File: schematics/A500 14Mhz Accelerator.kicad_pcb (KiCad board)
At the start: 2 copper layers, 120.6 x 54.6 mm, 17 parts, among them J1 Speed Selector, U1 68000 Boardside, U10 74HC74, U2 68HC000 Socket, U3 74HC86, U4 74HC74, U5 74LS27, U6 74LS112, U7 74HC04, U8 74LS157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

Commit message: Add files via upload
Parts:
- added C10: 0.1uF, Capacitor_THT:C_Axial_L3.8mm_D2.6mm_P7.50mm_Horizontal, F.Cu at (192.4, 130.2)
- added C4: 0.1uF, Capacitor_THT:C_Axial_L3.8mm_D2.6mm_P7.50mm_Horizontal, F.Cu at (182.2, 123.8)
- added C5: 0.1uF, Capacitor_THT:C_Axial_L3.8mm_D2.6mm_P7.50mm_Horizontal, F.Cu at (182.2, 127.0)
- added C6: 0.1uF, Capacitor_THT:C_Axial_L3.8mm_D2.6mm_P7.50mm_Horizontal, F.Cu at (182.2, 130.2)
- added C7: 0.1uF, Capacitor_THT:C_Axial_L3.8mm_D2.6mm_P7.50mm_Horizontal, F.Cu at (182.2, 133.3)
- added C8: 0.1uF, Capacitor_THT:C_Axial_L3.8mm_D2.6mm_P7.50mm_Horizontal, F.Cu at (192.4, 123.8)
- added C9: 0.1uF, Capacitor_THT:C_Axial_L3.8mm_D2.6mm_P7.50mm_Horizontal, F.Cu at (192.4, 127.0)
- C1: value 0.1uF -> 22pf
- C3: value 22pf -> 0.1uF
- moved C1 18.6 mm to (172.2, 132.7)
- moved C2 18.6 mm to (172.2, 135.9)
- moved U2 17.2 mm to (200.7, 102.9), turned to 270 degrees
- moved C3 13.2 mm to (179.7, 139.1), turned to 180 degrees
- moved J1 2.69 mm to (203.2, 128.9)
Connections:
- C1 pad 1: /VCC -> /GND
- C1 pad 2: /GND -> Net-(C1-Pad2)
- C2 pad 2: Net-(C2-Pad2) -> /A500 14Mhz Accelerator Sheet 2/CDAC
- C3 pad 1: /GND -> /VCC
- C3 pad 2: /A500 14Mhz Accelerator Sheet 2/CDAC -> /GND
- R1 pad 1: Net-(C2-Pad2) -> Net-(C1-Pad2)
- R2 pad 2: Net-(C2-Pad2) -> Net-(C1-Pad2)
- U3 pad 4: Net-(C2-Pad2) -> Net-(C1-Pad2)
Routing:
- net /CPU_A11: track 152.2 -> 81.9 mm, vias 2 -> 0
- net /CPU_A13: track 144.6 -> 76.8 mm
- net /CPU_E: track 153.9 -> 97.3 mm
- net /CPU_HALT: track 59.0 -> 99.3 mm, vias 0 -> 1
- net /CPU_DTACK14: track 54.1 -> 92.3 mm, vias 1 -> 0
- net Net-(C2-Pad2): track 37.8 -> 0.00 mm
- net /CPU_A17: track 107.3 -> 70.2 mm, vias 1 -> 0
- net /CPU_A19: track 104.9 -> 68.2 mm, vias 1 -> 0
- net /CPU_A15: track 111.1 -> 75.6 mm, vias 2 -> 0
- net /CPU_A16: track 102.6 -> 71.2 mm
- net Net-(C1-Pad2): track 0.00 -> 30.8 mm
- net /CPU_A4: track 124.7 -> 94.4 mm
- net /CPU_A22: track 95.2 -> 65.3 mm
- net /CPU_VPA14: track 104.4 -> 75.1 mm, vias 2 -> 0
- net /CPU_D4: track 22.4 -> 50.8 mm
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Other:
- board size 120.6 x 54.6 mm -> 121.9 x 55.9 mm
- board text added: "1"
- board text added: "14Mhz Accelerator (C) 1992 Livio Plos"
- board text added: "Hello Cave Dwellers!"

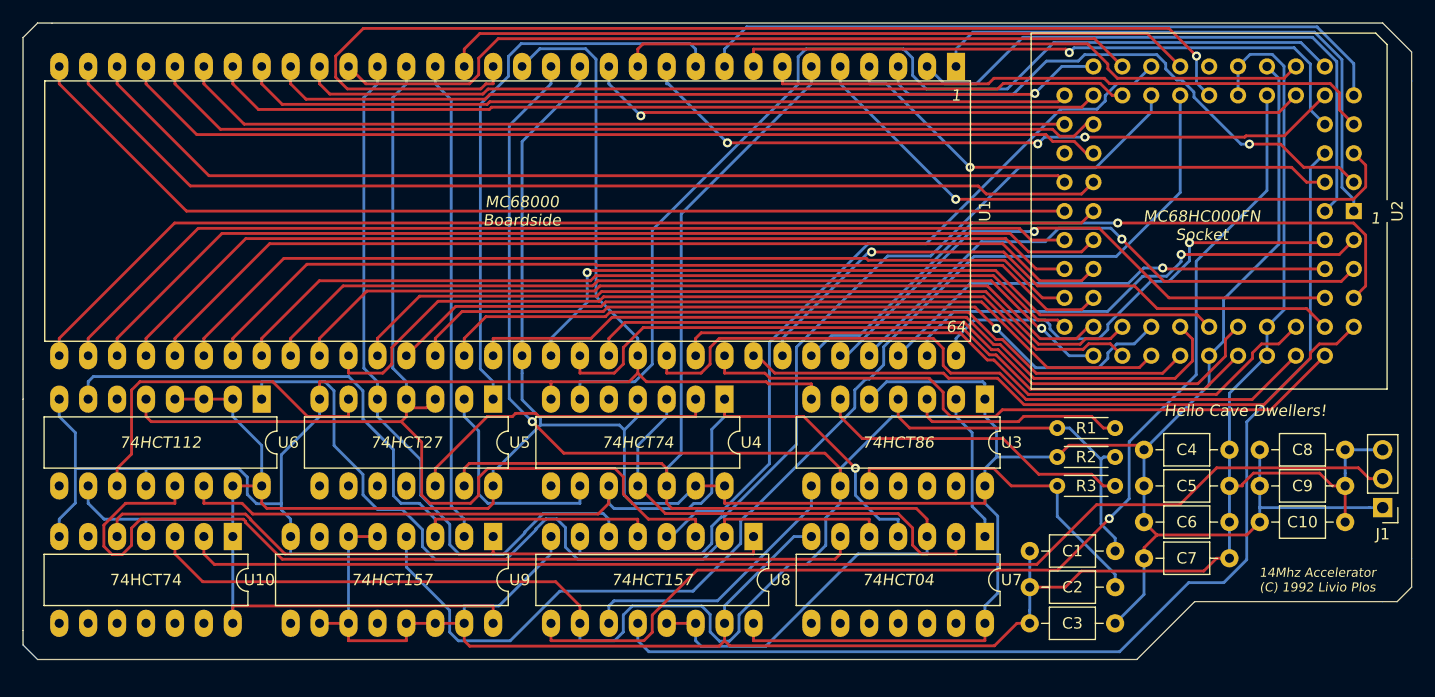
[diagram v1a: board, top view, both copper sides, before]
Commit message: Respin to add copper fill
Moved components around for better decoupling on the caps, added copper fill
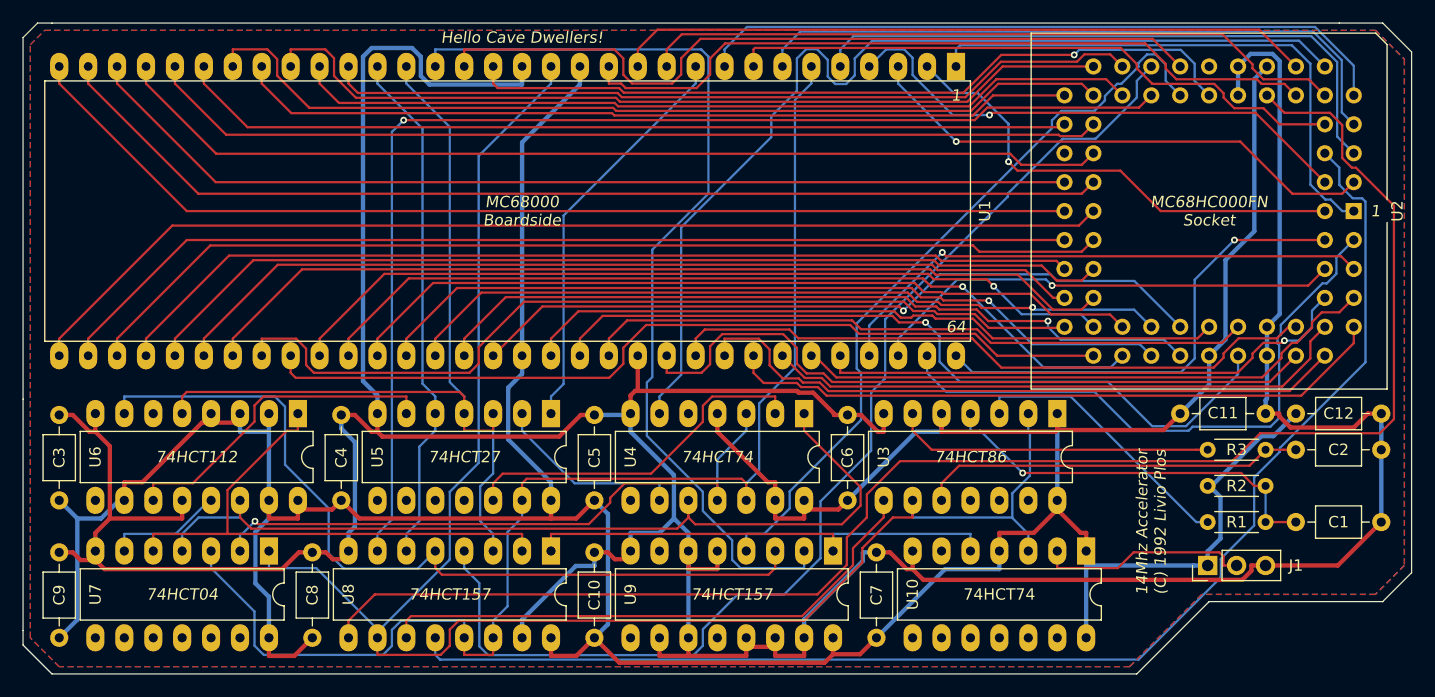
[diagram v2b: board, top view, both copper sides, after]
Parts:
- added C11: 0.1uF, Capacitor_THT:C_Axial_L3.8mm_D2.6mm_P7.50mm_Horizontal, F.Cu at (185.4, 120.7)
- added C12: 0.1uF, Capacitor_THT:C_Axial_L3.8mm_D2.6mm_P7.50mm_Horizontal, F.Cu at (195.6, 120.7)
- moved C9 106.3 mm to (87.0, 140.3), turned to 90 degrees
- moved C3 93.3 mm to (87.0, 128.3), turned to 90 degrees
- moved C8 84.8 mm to (109.2, 140.3), turned to 90 degrees
- moved U10 74.9 mm to (177.2, 132.7)
- moved C4 70.6 mm to (111.8, 128.3), turned to 90 degrees
- moved U7 62.9 mm to (105.4, 132.7)
- moved C10 59.3 mm to (134.0, 140.3), turned to 90 degrees
- moved C5 48.3 mm to (134.0, 128.3), turned to 90 degrees
- moved C2 33.1 mm to (203.1, 123.8), turned to 180 degrees
- moved C1 31.0 mm to (203.1, 130.2), turned to 180 degrees
- moved U9 29.9 mm to (154.9, 132.7)
- moved C6 26.1 mm to (156.2, 128.3), turned to 90 degrees
- moved C7 24.5 mm to (158.8, 140.3), turned to 90 degrees
- moved R1 20.1 mm to (192.9, 130.2), turned to 180 degrees
- moved R3 18.6 mm to (192.9, 123.8), turned to 180 degrees
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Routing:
- net /A500 14Mhz Accelerator Sheet 2/SPD_SEL: track 109.3 -> 18.8 mm
- net /A500 14Mhz Accelerator Sheet 2/_E_OUT: track 80.8 -> 10.3 mm
- net /CPU_VMA: track 42.3 -> 83.4 mm
- net /CPU_CLK14: track 98.8 -> 138.8 mm, vias 1 -> 0
- net /CPU_VMA14: track 102.3 -> 66.6 mm
- net /CPU_E14: track 66.2 -> 100.5 mm
- net /CPU_HALT: track 99.3 -> 68.8 mm
- net /CPU_VPA14: track 75.1 -> 105.3 mm, vias 0 -> 1
- net /A500 14Mhz Accelerator Sheet 2/SW_E14: track 74.0 -> 49.1 mm
- net /A500 14Mhz Accelerator Sheet 2/SW_CLK14: track 24.8 -> 49.5 mm
- net /CPU_AS14: track 97.3 -> 118.1 mm
- net /GND: track 342.9 -> 363.4 mm
- net /A500 14Mhz Accelerator Sheet 2/SEL_SW: track 62.1 -> 42.8 mm
- net /CPU_CLK: track 168.5 -> 150.0 mm, vias 1 -> 0
- net /CPU_E: track 97.3 -> 79.2 mm
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- added copper zone on F.Cu, net /GND
- added copper zone on B.Cu, net /VCC
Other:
- board size 121.9 x 55.9 mm -> 121.9 x 57.1 mm
- net class Default: trace_width 0.25 -> 0.2; via_dia 0.8 -> 0.6; via_drill 0.4 -> 0.3
- net class Power added: clearance 0.2, trace_width 0.381, via_dia 0.8, via_drill 0.4
- rule via_min_drill: 0.3 -> 0.2

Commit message: Reroute with correct socket
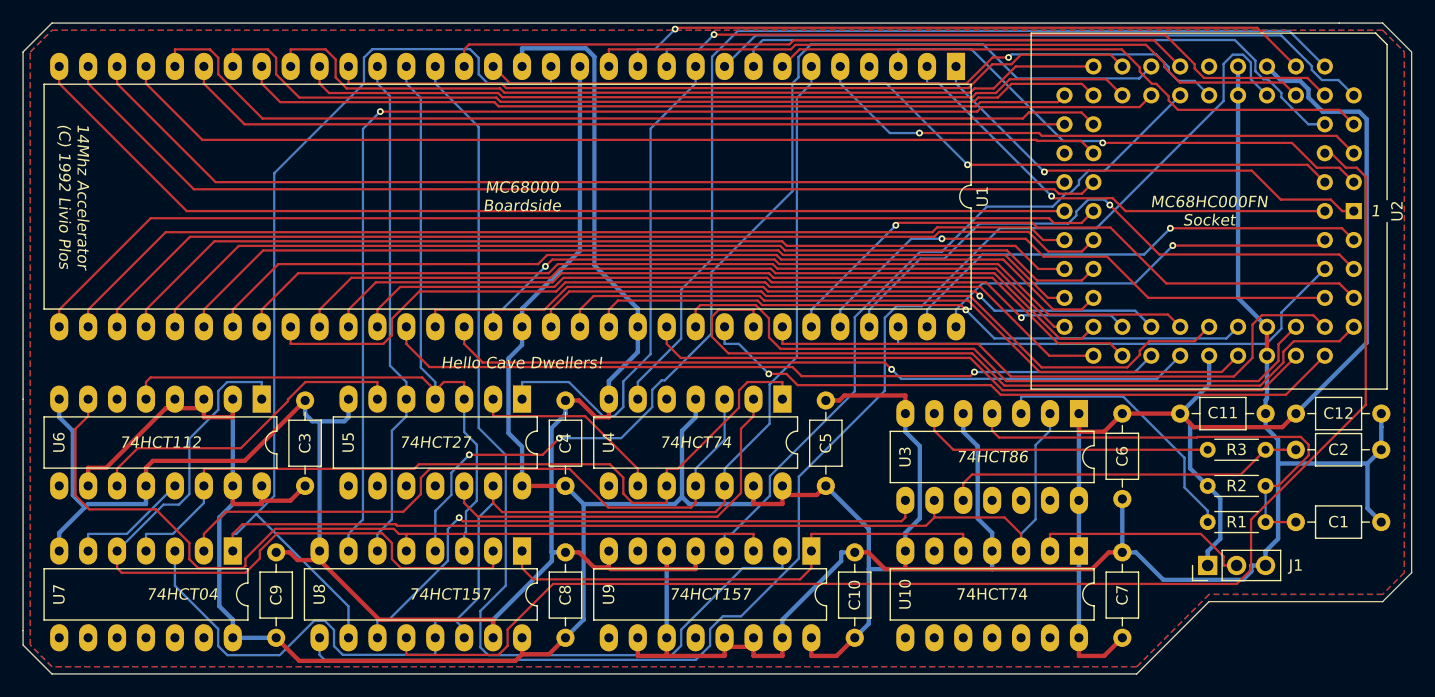
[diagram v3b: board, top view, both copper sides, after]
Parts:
- U1: footprint Package_DIP:DIP-64_W25.4mm_SIL_Headers -> Package_DIP:DIP-64_W22.86mm_LongPads
- moved U1 40.2 mm to (165.7, 90.2)
- moved C6 25.3 mm to (180.3, 120.7), turned to 270 degrees
- moved C10 22.9 mm to (156.8, 140.3)
- moved C8 22.2 mm to (131.4, 140.3)
- moved C3 21.6 mm to (108.6, 127.0)
- moved C7 21.6 mm to (180.3, 140.3)
- moved C5 20.4 mm to (154.3, 127.0)
- moved C4 19.7 mm to (131.4, 127.0)
- moved C9 19.0 mm to (106.0, 140.3)
- moved U6 3.42 mm to (104.8, 119.4)
- moved U7 3.17 mm to (102.2, 132.7)
- moved U5 2.84 mm to (127.6, 119.4)
- moved U8 2.54 mm to (127.6, 132.7)
- moved U4 2.29 mm to (150.5, 119.4)
- moved U3 1.91 mm to (176.5, 120.7)
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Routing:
- net /GND: track 363.4 -> 341.4 mm
- net /CPU_CLK: track 150.0 -> 171.0 mm
- net /CPU_CLK14: track 138.8 -> 119.9 mm
- net /A500 14Mhz Accelerator Sheet 2/SW_E14: track 49.1 -> 64.3 mm
- net /CPU_D6: track 53.7 -> 42.4 mm, vias 0 -> 1
- net /CPU_D12: track 58.4 -> 68.0 mm
- net /VCC: track 351.8 -> 342.7 mm
- net /CPU_DTACK: track 35.7 -> 44.5 mm
- net /CPU_D4: track 48.8 -> 41.2 mm, vias 0 -> 1
- net Net-(C1-Pad2): track 35.3 -> 41.5 mm, vias 1 -> 0
- net /CPU_D0: track 55.2 -> 49.1 mm, vias 0 -> 1
- net /CPU_A22: track 68.9 -> 63.1 mm, vias 1 -> 0
- net Net-(U4-Pad1): track 78.0 -> 72.4 mm
- net /A500 14Mhz Accelerator Sheet 2/SW_CLK14: track 49.5 -> 55.0 mm, vias 0 -> 1
- net /CPU_D5: track 41.8 -> 36.4 mm
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- added copper zone on B.Cu, net /GND
- removed copper zone on B.Cu, net /VCC
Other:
- outline, holes or cut-outs redrawn
